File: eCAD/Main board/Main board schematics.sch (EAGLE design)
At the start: 65 parts, among them IC1 ESP32-WROOM-32E_M113EH3200PH3Q, IC2 TP4056X, IC3 DW01A-G, IC4 ME6211C33M5G-N, IC5 ME6211C33M5G-N, J1 XT30PW-M, Q1 IRF7319TRPBF, Q2 IRF7319TRPBF, Q3 SI2347DS-T1-GE3, Q4 FS8205A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

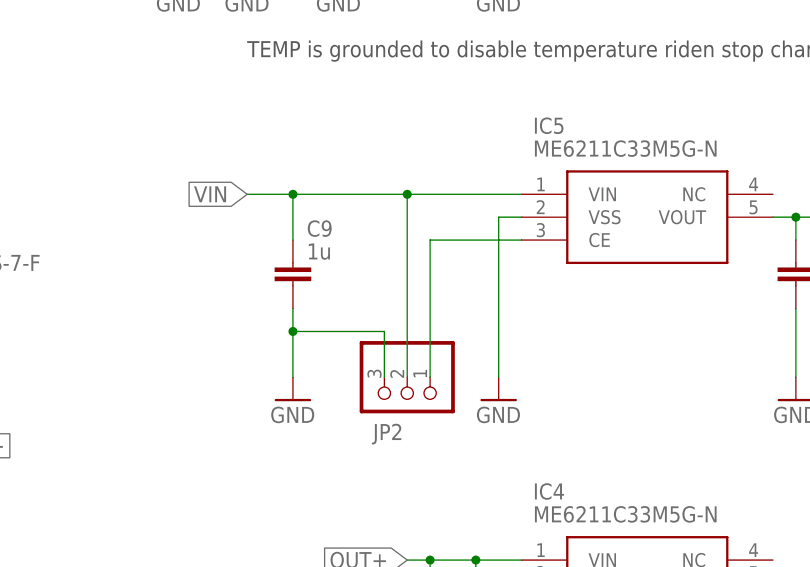
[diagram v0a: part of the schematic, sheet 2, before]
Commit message: Repair mistakes: C2, flash pin on ESP, fan pinout
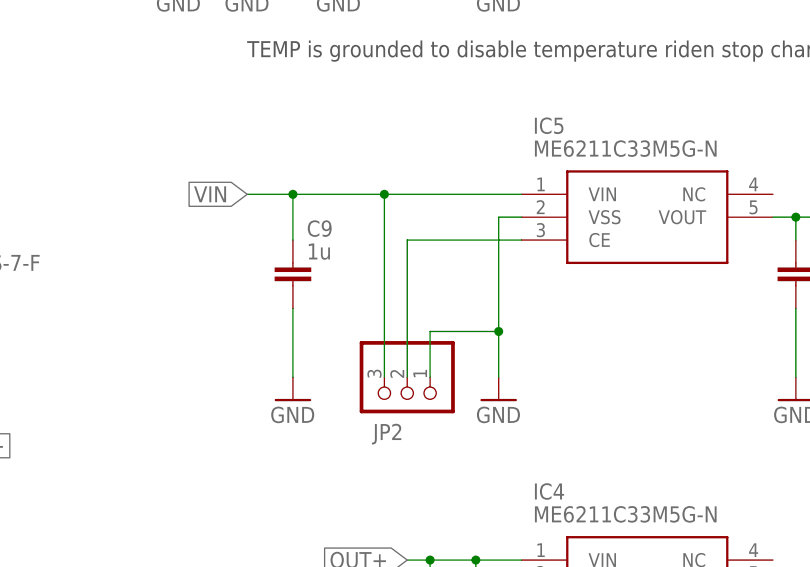
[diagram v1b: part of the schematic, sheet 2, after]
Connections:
- net ESP_FLASH: now also IC1.IO0; no longer IC1.IO2
- net GND: now also C11.-, JP2.1; no longer C11.+, JP2.3
- net N$6: now also JP2.2; no longer JP2.1
- net VDD33: now also C11.+; no longer C11.-
- net VIN: now also JP2.3; no longer JP2.2
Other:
- moved on the sheet: C11
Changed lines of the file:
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@@
 <attribute name="VALUE" x="149.86" y="12.7" size="1.778" layer="96"/>
 </instance>
-<instance part="C11" gate="G$1" x="35.56" y="152.4" smashed="yes">
+<instance part="C11" gate="G$1" x="35.56" y="149.86" smashed="yes" rot="R180">
 <attribute name="NAME" x="36.703" y="152.8826" size="1.778" layer="95"/>
 <attribute name="VALUE" x="36.703" y="147.8026" size="1.778" layer="96"/>
@@
 <junction x="45.72" y="157.48"/>
 <label x="53.34" y="157.48" size="1.778" layer="95" rot="R90" xref="yes"/>
-<pinref part="C11" gate="G$1" pin="+"/>
+<pinref part="IC1" gate="G$1" pin="GND_1"/>
+<pinref part="C11" gate="G$1" pin="-"/>
 <wire x1="35.56" y1="154.94" x2="35.56" y2="157.48" width="0.1524" layer="91"/>
-<pinref part="IC1" gate="G$1" pin="GND_1"/>
 </segment>
 <segment>
@@
 </segment>
 <segment>
-<wire x1="55.88" y1="88.9" x2="53.34" y2="88.9" width="0.1524" layer="91"/>
-<label x="53.34" y="88.9" size="1.778" layer="95" rot="R180"/>
-<pinref part="IC1" gate="G$1" pin="IO2"/>
+<pinref part="IC1" gate="G$1" pin="IO0"/>
+<wire x1="93.98" y1="147.32" x2="96.52" y2="147.32" width="0.1524" layer="91"/>
+<label x="96.52" y="147.32" size="1.778" layer="95"/>
 </segment>
 </net>
@@
 <wire x1="45.72" y1="147.32" x2="45.72" y2="144.78" width="0.1524" layer="91"/>
 <junction x="45.72" y="144.78"/>
-<pinref part="C11" gate="G$1" pin="-"/>
+<pinref part="IC1" gate="G$1" pin="3V3"/>
+<pinref part="C11" gate="G$1" pin="+"/>
 <wire x1="35.56" y1="147.32" x2="35.56" y2="144.78" width="0.1524" layer="91"/>
 <junction x="35.56" y="144.78"/>
-<pinref part="IC1" gate="G$1" pin="3V3"/>
 </segment>
 <segment>
@@
 <pinref part="GND27" gate="1" pin="GND"/>
 <pinref part="C9" gate="G$1" pin="2"/>
-<wire x1="152.4" y1="88.9" x2="152.4" y2="86.36" width="0.1524" layer="91"/>
-<pinref part="JP2" gate="A" pin="3"/>
-<wire x1="152.4" y1="86.36" x2="152.4" y2="81.28" width="0.1524" layer="91"/>
-<wire x1="162.56" y1="81.28" x2="162.56" y2="86.36" width="0.1524" layer="91"/>
-<wire x1="162.56" y1="86.36" x2="152.4" y2="86.36" width="0.1524" layer="91"/>
-<junction x="152.4" y="86.36"/>
+<wire x1="152.4" y1="88.9" x2="152.4" y2="81.28" width="0.1524" layer="91"/>
 </segment>
 <segment>
@@
 <segment>
 <wire x1="177.8" y1="99.06" x2="175.26" y2="99.06" width="0.1524" layer="91"/>
-<wire x1="175.26" y1="99.06" x2="175.26" y2="81.28" width="0.1524" layer="91"/>
+<wire x1="175.26" y1="99.06" x2="175.26" y2="86.36" width="0.1524" layer="91"/>
 <pinref part="GND25" gate="1" pin="GND"/>
 <pinref part="IC5" gate="G$1" pin="VSS"/>
+<pinref part="JP2" gate="A" pin="1"/>
+<wire x1="175.26" y1="86.36" x2="175.26" y2="81.28" width="0.1524" layer="91"/>
+<wire x1="167.64" y1="81.28" x2="167.64" y2="86.36" width="0.1524" layer="91"/>
+<wire x1="167.64" y1="86.36" x2="175.26" y2="86.36" width="0.1524" layer="91"/>
+<junction x="175.26" y="86.36"/>
 </segment>
 <segment>
@@
 </segment>
 <segment>
-<wire x1="177.8" y1="101.6" x2="165.1" y2="101.6" width="0.1524" layer="91"/>
 <pinref part="C9" gate="G$1" pin="1"/>
-<wire x1="165.1" y1="101.6" x2="152.4" y2="101.6" width="0.1524" layer="91"/>
+<wire x1="177.8" y1="101.6" x2="162.56" y2="101.6" width="0.1524" layer="91"/>
+<wire x1="162.56" y1="101.6" x2="152.4" y2="101.6" width="0.1524" layer="91"/>
 <wire x1="152.4" y1="101.6" x2="152.4" y2="96.52" width="0.1524" layer="91"/>
 <pinref part="IC5" gate="G$1" pin="VIN"/>
@@
 <junction x="152.4" y="101.6"/>
 <label x="147.32" y="101.6" size="1.778" layer="95" rot="R180" xref="yes"/>
-<pinref part="JP2" gate="A" pin="2"/>
-<wire x1="165.1" y1="81.28" x2="165.1" y2="101.6" width="0.1524" layer="91"/>
-<junction x="165.1" y="101.6"/>
+<pinref part="JP2" gate="A" pin="3"/>
+<wire x1="162.56" y1="81.28" x2="162.56" y2="101.6" width="0.1524" layer="91"/>
+<junction x="162.56" y="101.6"/>
 </segment>
 <segment>
@@
 <net name="N$6" class="0">
 <segment>
-<pinref part="JP2" gate="A" pin="1"/>
 <pinref part="IC5" gate="G$1" pin="CE"/>
-<wire x1="167.64" y1="81.28" x2="167.64" y2="96.52" width="0.1524" layer="91"/>
-<wire x1="167.64" y1="96.52" x2="177.8" y2="96.52" width="0.1524" layer="91"/>
-</segment>
-</net>
+<wire x1="165.1" y1="96.52" x2="177.8" y2="96.52" width="0.1524" layer="91"/>
+<pinref part="JP2" gate="A" pin="2"/>
+<wire x1="165.1" y1="96.52" x2="165.1" y2="81.28" width="0.1524" layer="91"/>
+</segment>
+</net>
